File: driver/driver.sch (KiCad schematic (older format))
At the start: 24 parts, among them J1 Screw_Terminal_01x04, J2 Screw_Terminal_01x04, J3 Conn_01x03_Female, J4 Conn_01x03_Female, J5 Barrel_Jack, SW1 SW_SPDT, SW2 SW_SPDT, SW3 SW_SPDT, U1 NCP1117ST50T3G

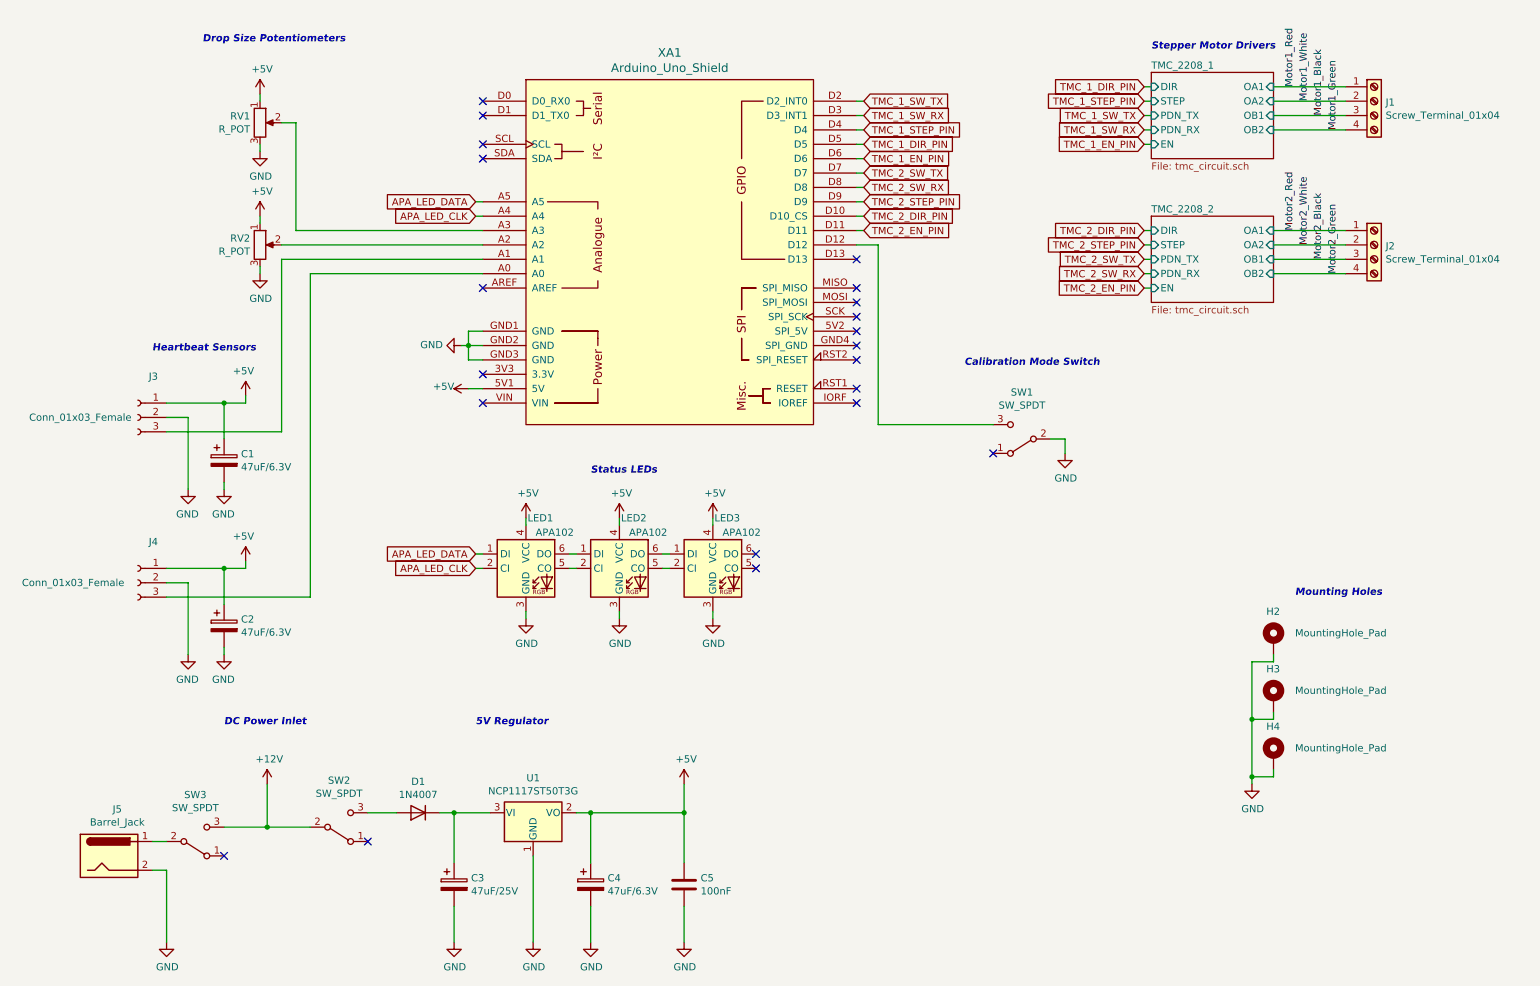
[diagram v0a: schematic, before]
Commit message: Added BOM, re-organized things a bit
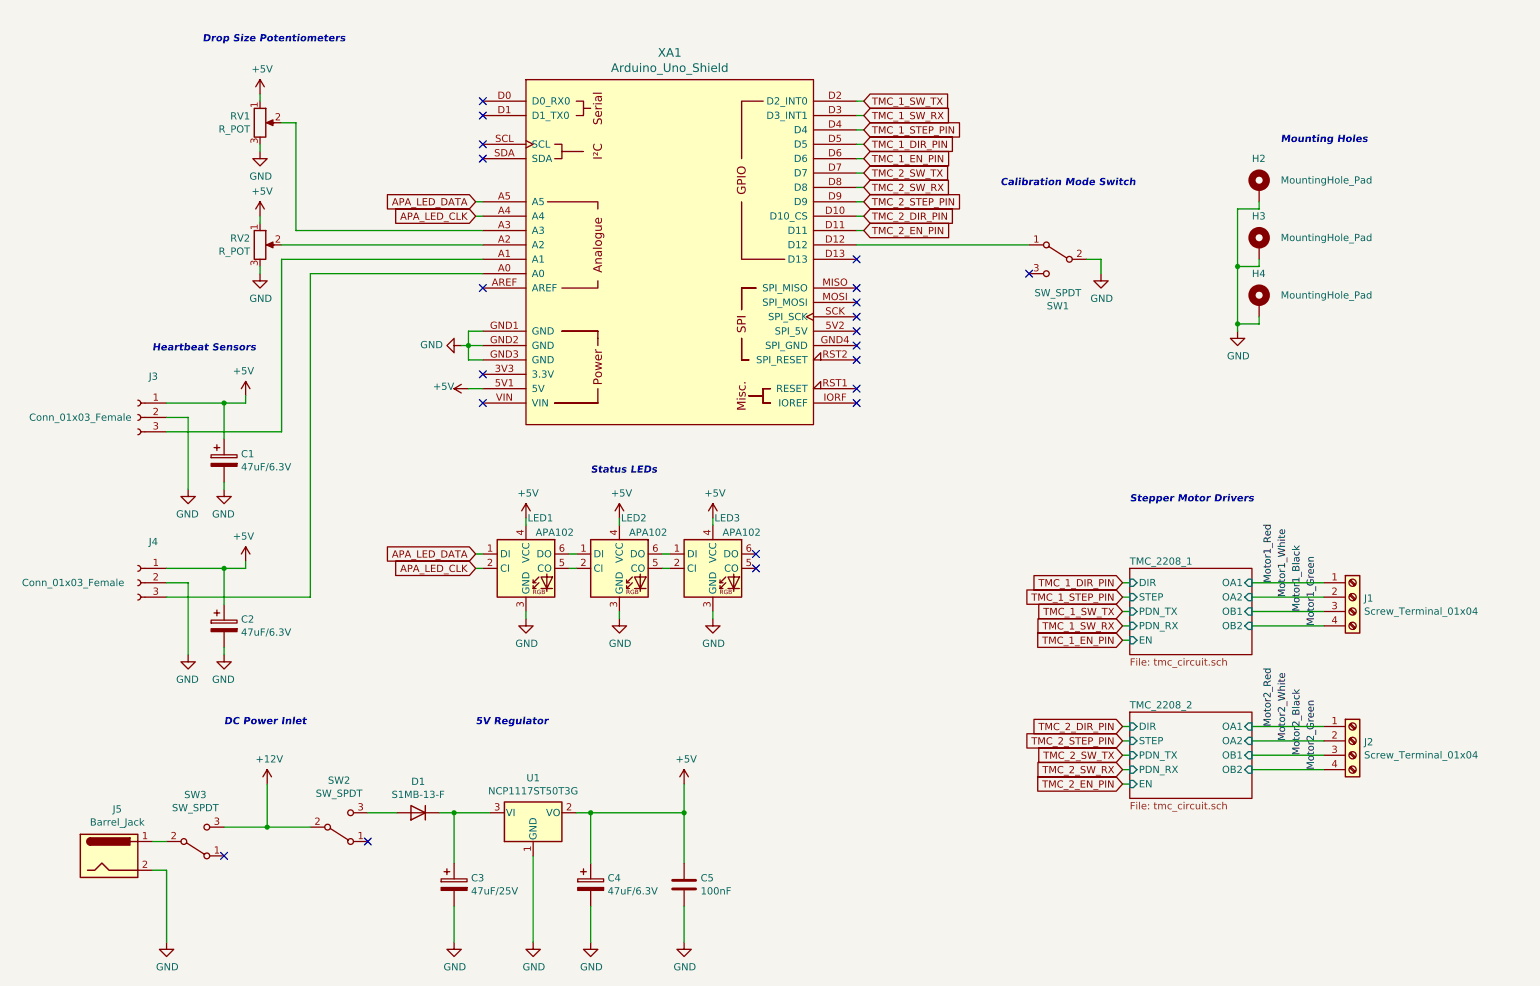
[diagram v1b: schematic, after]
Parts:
- C5: footprint Capacitor_SMD:C_0201_0603Metric_Pad0.64x0.40mm_HandSolder -> Capacitor_SMD:C_0805_2012Metric_Pad1.18x1.45mm_HandSolder; Digi-Key Part Number 1276-1013-1-ND -> 478-08056D104KAT2ACT-ND
- D1: value 1N4007 -> S1MB-13-F; footprint Diode_THT:D_DO-41_SOD81_P10.16mm_Horizontal -> Diode_SMD:D_SMB; Digi-Key Part Number (none) -> S1MB-FDICT-ND
- LED1, LED2, LED3: Digi-Key Part Number (none) -> 2007-BB-HBGR32L-3-TRB-8CT-ND
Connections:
- net at XA1.D12: now also SW1.1 (A); no longer SW1.3 (C)
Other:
- moved on the sheet: H2, H3, H4, J1, J2, SW1

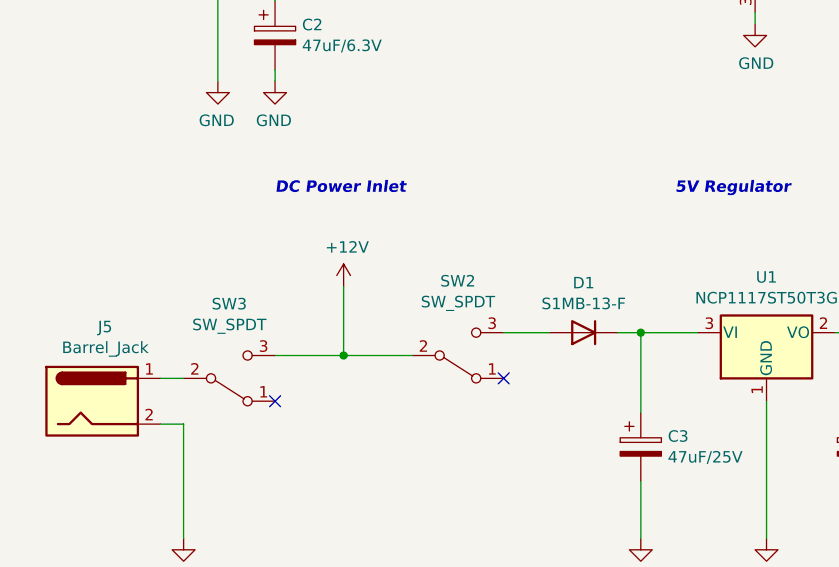
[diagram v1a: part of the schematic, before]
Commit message: Routed both boards, happy. Hopefully the traces are thick enough, used an only calculator given max rated draw of the TMCs
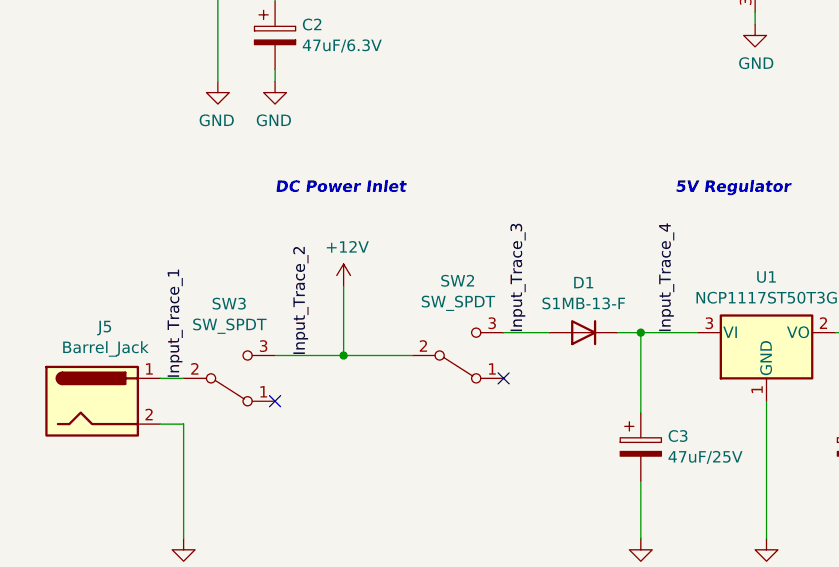
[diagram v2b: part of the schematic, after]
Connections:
- net Input_Trace_1: now reaches J5.1, SW3.2 (B)
- net Input_Trace_4: now reaches C3.1, D1.1 (K), U1.3 (VI)
- net Input_Trace_3: now reaches D1.2 (A), SW2.3 (C)
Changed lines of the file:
@@
 Text GLabel 3850 4300 0    50   Input ~ 0
 APA_LED_DATA
+Text Label 1700 6300 1    50   ~ 0
+Input_Trace_1
+Text Label 2250 6200 1    50   ~ 0
+Input_Trace_2
+Text Label 3200 6100 1    50   ~ 0
+Input_Trace_3
+Text Label 3850 6100 1    50   ~ 0
+Input_Trace_4
 $EndSCHEMATC

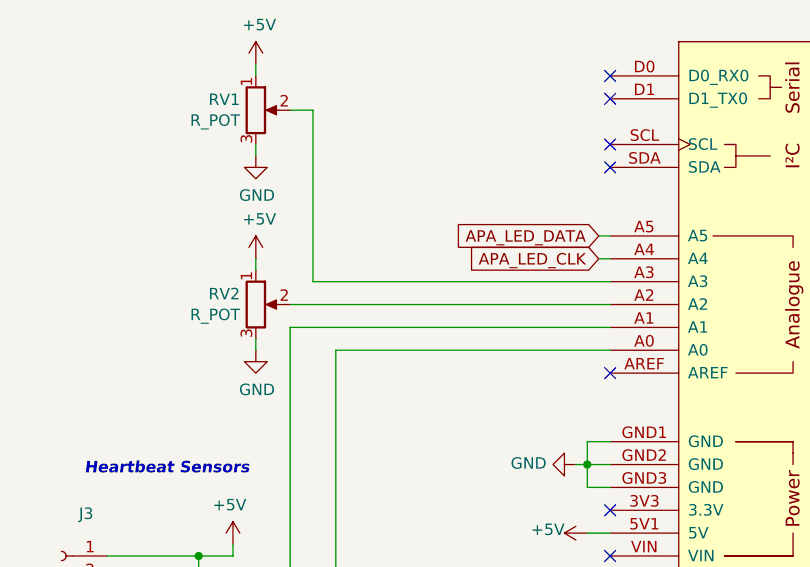
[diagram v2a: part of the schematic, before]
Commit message: Fit test passed, panelized boards. Ready to order soon
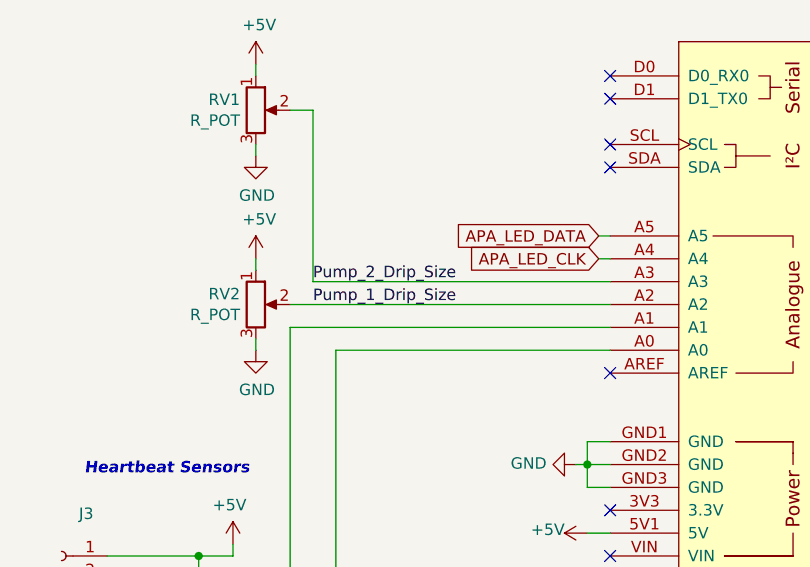
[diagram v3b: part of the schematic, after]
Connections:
- net Pump_1_Drip_Size: now reaches RV2.2, XA1.A2
- net Pump_2_Drip_Size: now reaches RV1.2, XA1.A3
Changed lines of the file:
@@
 Text Label 3850 6100 1    50   ~ 0
 Input_Trace_4
+Text Label 2600 2150 0    50   ~ 0
+Pump_1_Drip_Size
+Text Label 2600 2050 0    50   ~ 0
+Pump_2_Drip_Size
 $EndSCHEMATC

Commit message: Design is finished, ordering boards
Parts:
- added C8: 100uF, Capacitor_SMD:CP_Elec_6.3x5.8, symbol Device:CP
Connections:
- net GND: now also C8.2
- net Input_Trace_1: now also C8.1
- net PULSE1_PIN: now reaches J4.3 (Pin_3), XA1.A0
- net PULSE2_PIN: now reaches J3.3 (Pin_3), XA1.A1
- net APA_LED_CLK renamed LED_CLOCK_PIN
- net APA_LED_DATA renamed LED_DATA_PIN
- net Pump_1_Drip_Size renamed PUMP_1_DRIP_SIZE_POT_PIN
- net Pump_2_Drip_Size renamed PUMP_2_DRIP_SIZE_POT_PIN
- net TMC_1_SW_RX renamed TMC_1_SW_RX_PIN
- net TMC_1_SW_TX renamed TMC_1_SW_TX_PIN
- net TMC_2_SW_RX renamed TMC_2_SW_RX_PIN
- net TMC_2_SW_TX renamed TMC_2_SW_TX_PIN
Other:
- moved on the sheet: J5, LED1, LED2, LED3
